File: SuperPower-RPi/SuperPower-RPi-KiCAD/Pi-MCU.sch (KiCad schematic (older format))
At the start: 14 parts, among them J5 Conn_01x06, SW1 Tact, U3 STM32F412RGTx, U4 ATtiny1614-SS, U5 ME6210A33M3G

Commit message: Part Meta-data updates continued.
(cherry picked from commit d0ad2c93dfb1e315a7dc98683a53ed7dcb5f49ff)
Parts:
- added J7: Conn_01x03, symbol Connector_Generic:Conn_01x03
- C25: value 0.1uF -> DNP
- R15: value 10k -> DNP
- U3: Mfg (none) -> ST
- U4: value ATtiny1614-SS -> DNP; Mfg (none) -> MicroChip; Mfg PN (none) -> ATTINY1614-SSFR
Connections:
- net labels removed: Reset
- wire segments 83 -> 92
- no-connect marks 1 -> 0
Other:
- note added: "ATTiny Programming\nVia UPDI"
- note added: "ATtiny1614-SS\n(Optional instead of STM)"
- moved on the sheet: C24, C25, R15, SW1
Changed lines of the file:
@@
 Text HLabel 4950 3000 2    50   BiDi ~ 0
 SCL
-Text HLabel 2350 4100 0    50   BiDi ~ 0
+Text HLabel 3150 3700 0    50   BiDi ~ 0
 GPIO0
-NoConn ~ 2350 4100
 Text Notes 1000 7200 0    50   ~ 0
 Add jumper for measuring MCU current.
@@
 F 2 "Package_QFP:LQFP-64_10x10mm_P0.5mm" H 3500 2000 50  0001 R CNN
 F 3 "http://www.st.com/st-web-ui/static/active/en/resource/technical/document/datasheet/DM00213872.pdf" H 4100 3700 50  0001 C CNN
+F 4 "ST" H 4100 3700 50  0001 C CNN "Mfg"
 	1    4100 3700
-	1    0    0    -1
-$EndComp
-$Comp
-L MCU_Microchip_ATtiny:ATtiny1614-SS U4
-U 1 1 5F9378C2
-P 8750 3950
-F 0 "U4" H 8750 4050 50  0000 C CNN
-F 1 "ATtiny1614-SS" H 8750 3900 50  0000 C CNN
-F 2 "Package_SO:SOIC-14_3.9x8.7mm_P1.27mm" H 8750 3950 50  0001 C CIN
-F 3 "http://ww1.microchip.com/downloads/en/DeviceDoc/ATtiny1614-data-sheet-40001995A.pdf" H 8750 3950 50  0001 C CNN
-	1    8750 3950
 	1    0    0    -1
 $EndComp
@@
 L power:+3.3V #PWR025
 U 1 1 5FA2A2A7
-P 8750 3050
-F 0 "#PWR025" H 8750 2900 50  0001 C CNN
-F 1 "+3.3V" H 8765 3223 50  0000 C CNN
-F 2 "" H 8750 3050 50  0001 C CNN
-F 3 "" H 8750 3050 50  0001 C CNN
-	1    8750 3050
-	1    0    0    -1
-$EndComp
-Wire Wire Line
-	8750 3250 8750 3050
+P 8550 3000
+F 0 "#PWR025" H 8550 2850 50  0001 C CNN
+F 1 "+3.3V" H 8565 3173 50  0000 C CNN
+F 2 "" H 8550 3000 50  0001 C CNN
+F 3 "" H 8550 3000 50  0001 C CNN
+	1    8550 3000
+	1    0    0    -1
+$EndComp
 $Comp
 L Device:C_Small C25
 U 1 1 5FA2B8E5
-P 9250 2900
-F 0 "C25" H 9158 2854 50  0000 R CNN
-F 1 "0.1uF" H 9158 2945 50  0000 R CNN
-F 2 "Capacitor_SMD:C_0603_1608Metric" H 9250 2900 50  0001 C CNN
-F 3 "~" H 9250 2900 50  0001 C CNN
-	1    9250 2900
-	-1   0    0    1
+P 8850 3050
+F 0 "C25" V 8800 3250 50  0000 R CNN
+F 1 "DNP" V 8800 3000 50  0000 R CNN
+F 2 "Capacitor_SMD:C_0603_1608Metric" H 8850 3050 50  0001 C CNN
+F 3 "~" H 8850 3050 50  0001 C CNN
+	1    8850 3050
+	0    -1   1    0
 $EndComp
 $Comp
@@
 L power:GND #PWR026
 U 1 1 5FA2E9B4
-P 8750 4750
-F 0 "#PWR026" H 8750 4500 50  0001 C CNN
-F 1 "GND" H 8755 4577 50  0000 C CNN
-F 2 "" H 8750 4750 50  0001 C CNN
-F 3 "" H 8750 4750 50  0001 C CNN
-	1    8750 4750
-	1    0    0    -1
-$EndComp
-Text HLabel 9600 3650 2    50   BiDi ~ 0
+P 8550 4750
+F 0 "#PWR026" H 8550 4500 50  0001 C CNN
+F 1 "GND" H 8555 4577 50  0000 C CNN
+F 2 "" H 8550 4750 50  0001 C CNN
+F 3 "" H 8550 4750 50  0001 C CNN
+	1    8550 4750
+	1    0    0    -1
+$EndComp
+Text HLabel 9400 3650 2    50   BiDi ~ 0
 SDA
 Wire Wire Line
-	9600 3650 9350 3650
-Text HLabel 9600 3750 2    50   BiDi ~ 0
+	9400 3650 9150 3650
+Text HLabel 9400 3750 2    50   BiDi ~ 0
 SCL
 Wire Wire Line
-	9600 3750 9350 3750
+	9400 3750 9150 3750
 $Comp
 L power:+3.3V #PWR027
 U 1 1 5FA2FF44
-P 9600 3250
-F 0 "#PWR027" H 9600 3100 50  0001 C CNN
-F 1 "+3.3V" H 9615 3423 50  0000 C CNN
-F 2 "" H 9600 3250 50  0001 C CNN
-F 3 "" H 9600 3250 50  0001 C CNN
-	1    9600 3250
+P 9400 3250
+F 0 "#PWR027" H 9400 3100 50  0001 C CNN
+F 1 "+3.3V" H 9415 3423 50  0000 C CNN
+F 2 "" H 9400 3250 50  0001 C CNN
+F 3 "" H 9400 3250 50  0001 C CNN
+	1    9400 3250
 	1    0    0    -1
 $EndComp
@@
 L Device:R_Small R15
 U 1 1 5FA305E2
-P 9600 3400
-F 0 "R15" H 9659 3446 50  0000 L CNN
-F 1 "10k" H 9659 3355 50  0000 L CNN
-F 2 "Resistor_SMD:R_0603_1608Metric" H 9600 3400 50  0001 C CNN
-F 3 "~" H 9600 3400 50  0001 C CNN
-	1    9600 3400
-	1    0    0    -1
-$EndComp
-Wire Wire Line
-	9600 3300 9600 3250
-Wire Wire Line
-	9350 3550 9600 3550
-Wire Wire Line
-	9600 3550 9600 3500
-Wire Wire Line
-	9600 3550 9850 3550
-Connection ~ 9600 3550
-Text Label 9850 3550 0    50   ~ 0
-Reset
-Wire Wire Line
-	8750 4650 8750 4750
-Text HLabel 7750 3900 0    50   BiDi ~ 0
+P 9400 3400
+F 0 "R15" H 9459 3446 50  0000 L CNN
+F 1 "DNP" H 9459 3355 50  0000 L CNN
+F 2 "Resistor_SMD:R_0603_1608Metric" H 9400 3400 50  0001 C CNN
+F 3 "~" H 9400 3400 50  0001 C CNN
+	1    9400 3400
+	1    0    0    -1
+$EndComp
+Wire Wire Line
+	9400 3300 9400 3250
+Wire Wire Line
+	9150 3550 9400 3550
+Wire Wire Line
+	9400 3550 9400 3500
+Wire Wire Line
+	9400 3550 9650 3550
+Connection ~ 9400 3550
+Wire Wire Line
+	8550 4650 8550 4750
+Text HLabel 7550 3900 0    50   BiDi ~ 0
 GPIO0
 Text Label 5250 3500 2    50   ~ 0
@@
 L Switch:SW_Push SW1
 U 1 1 5FA488EA
-P 6700 5500
-F 0 "SW1" V 6746 5452 50  0000 R CNN
-F 1 "Tact" V 6655 5452 50  0000 R CNN
-F 2 "" H 6700 5700 50  0001 C CNN
-F 3 "~" H 6700 5700 50  0001 C CNN
-	1    6700 5500
+P 1200 5750
+F 0 "SW1" V 1246 5702 50  0000 R CNN
+F 1 "Tact" V 1155 5702 50  0000 R CNN
+F 2 "" H 1200 5950 50  0001 C CNN
+F 3 "~" H 1200 5950 50  0001 C CNN
+	1    1200 5750
 	0    -1   -1   0
 $EndComp
@@
 L Device:C_Small C24
 U 1 1 5FA4ADCC
-P 7050 5500
-F 0 "C24" H 6958 5454 50  0000 R CNN
-F 1 "0.1uF" H 6958 5545 50  0000 R CNN
-F 2 "Capacitor_SMD:C_0603_1608Metric" H 7050 5500 50  0001 C CNN
-F 3 "~" H 7050 5500 50  0001 C CNN
-	1    7050 5500
+P 1550 5750
+F 0 "C24" H 1458 5704 50  0000 R CNN
+F 1 "0.1uF" H 1458 5795 50  0000 R CNN
+F 2 "Capacitor_SMD:C_0603_1608Metric" H 1550 5750 50  0001 C CNN
+F 3 "~" H 1550 5750 50  0001 C CNN
+	1    1550 5750
 	-1   0    0    1
 $EndComp
@@
 L power:GND #PWR024
 U 1 1 5FA4B4BE
-P 6800 5900
-F 0 "#PWR024" H 6800 5650 50  0001 C CNN
-F 1 "GND" H 6805 5727 50  0000 C CNN
-F 2 "" H 6800 5900 50  0001 C CNN
-F 3 "" H 6800 5900 50  0001 C CNN
-	1    6800 5900
-	1    0    0    -1
-$EndComp
-Wire Wire Line
-	6800 5900 6800 5800
-Wire Wire Line
-	6800 5800 6700 5800
-Wire Wire Line
-	6700 5800 6700 5700
-Wire Wire Line
-	6800 5800 7050 5800
-Wire Wire Line
-	7050 5800 7050 5600
-Connection ~ 6800 5800
-Text Label 7100 5200 0    50   ~ 0
+P 1300 6150
+F 0 "#PWR024" H 1300 5900 50  0001 C CNN
+F 1 "GND" H 1305 5977 50  0000 C CNN
+F 2 "" H 1300 6150 50  0001 C CNN
+F 3 "" H 1300 6150 50  0001 C CNN
+	1    1300 6150
+	1    0    0    -1
+$EndComp
+Wire Wire Line
+	1300 6150 1300 6050
+Wire Wire Line
+	1300 6050 1200 6050
+Wire Wire Line
+	1200 6050 1200 5950
+Wire Wire Line
+	1300 6050 1550 6050
+Wire Wire Line
+	1550 6050 1550 5850
+Connection ~ 1300 6050
+Text Label 1600 5450 0    50   ~ 0
 nRESET
 Wire Wire Line
-	7050 5400 7050 5200
-Wire Wire Line
-	7050 5200 6700 5200
-Wire Wire Line
-	6700 5200 6700 5300
-Wire Wire Line
-	7100 5200 7050 5200
-Connection ~ 7050 5200
+	1550 5650 1550 5450
+Wire Wire Line
+	1550 5450 1200 5450
+Wire Wire Line
+	1200 5450 1200 5550
+Wire Wire Line
+	1600 5450 1550 5450
+Connection ~ 1550 5450
 Wire Wire Line
 	4400 2000 4400 1900
@@
 Wire Wire Line
 	4150 5600 4100 5600
+$Comp
+L MCU_Microchip_ATtiny:ATtiny1614-SS U4
+U 1 1 5F9378C2
+P 8550 3950
+F 0 "U4" H 8550 4050 50  0000 C CNN
+F 1 "DNP" H 8550 3900 50  0000 C CNN
+F 2 "Package_SO:SOIC-14_3.9x8.7mm_P1.27mm" H 8550 3950 50  0001 C CIN
+F 3 "http://ww1.microchip.com/downloads/en/DeviceDoc/ATtiny1614-data-sheet-40001995A.pdf" H 8550 3950 50  0001 C CNN
+F 4 "MicroChip" H 8550 3950 50  0001 C CNN "Mfg"
+F 5 "ATTINY1614-SSFR" H 8550 3950 50  0001 C CNN "Mfg PN"
+	1    8550 3950
+	1    0    0    -1
+$EndComp
+Text Notes 8300 5250 0    50   ~ 0
+ATtiny1614-SS\n(Optional instead of STM)
+Wire Wire Line
+	8750 3050 8550 3050
+Connection ~ 8550 3050
+Wire Wire Line
+	8550 3050 8550 3000
+$Comp
+L power:GND #PWR029
+U 1 1 5FA31170
+P 9050 3100
+F 0 "#PWR029" H 9050 2850 50  0001 C CNN
+F 1 "GND" H 9055 2927 50  0000 C CNN
+F 2 "" H 9050 3100 50  0001 C CNN
+F 3 "" H 9050 3100 50  0001 C CNN
+	1    9050 3100
+	1    0    0    -1
+$EndComp
+Wire Wire Line
+	8550 3050 8550 3250
+Wire Wire Line
+	9050 3100 9050 3050
+Wire Wire Line
+	9050 3050 8950 3050
+$Comp
+L Connector_Generic:Conn_01x03 J7
+U 1 1 5FA390FB
+P 10550 4900
+F 0 "J7" H 10630 4896 50  0000 L CNN
+F 1 "Conn_01x03" H 10630 4851 50  0001 L CNN
+F 2 "" H 10550 4900 50  0001 C CNN
+F 3 "~" H 10550 4900 50  0001 C CNN
+	1    10550 4900
+	1    0    0    -1
+$EndComp
+$Comp
+L power:GND #PWR031
+U 1 1 5FA3A649
+P 10250 5100
+F 0 "#PWR031" H 10250 4850 50  0001 C CNN
+F 1 "GND" H 10255 4927 50  0000 C CNN
+F 2 "" H 10250 5100 50  0001 C CNN
+F 3 "" H 10250 5100 50  0001 C CNN
+	1    10250 5100
+	1    0    0    -1
+$EndComp
+Wire Wire Line
+	10250 5100 10250 4900
+Wire Wire Line
+	10250 4900 10350 4900
+$Comp
+L power:+3.3V #PWR030
+U 1 1 5FA3CED7
+P 10250 4700
+F 0 "#PWR030" H 10250 4550 50  0001 C CNN
+F 1 "+3.3V" H 10265 4873 50  0000 C CNN
+F 2 "" H 10250 4700 50  0001 C CNN
+F 3 "" H 10250 4700 50  0001 C CNN
+	1    10250 4700
+	1    0    0    -1
+$EndComp
+Wire Wire Line
+	10350 4800 10250 4800
+Wire Wire Line
+	10250 4800 10250 4700
+Wire Wire Line
+	10350 5000 9900 5000
+Text Notes 9950 5600 0    50   ~ 0
+ATTiny Programming\nVia UPDI
+Text Label 9900 5000 0    50   ~ 0
+nRESET
+Text Label 9650 3550 0    50   ~ 0
+nRESET
 $EndSCHEMATC

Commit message: Added local footprint library, and associated components.
(cherry picked from commit 78b1abfd5fe55b90039e798d35239acda24b0417)
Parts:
- added C29, C31: 0.1uF, Capacitor_SMD:C_0603_1608Metric, symbol Device:C_Small
- added C30: 10nF, Capacitor_SMD:C_0603_1608Metric, symbol Device:C_Small
- added C32: 1.0uF, Capacitor_SMD:C_0603_1608Metric, symbol Device:C_Small
- added J8: Conn_01x10, Connector_PinHeader_2.54mm:PinHeader_1x10_P2.54mm_Vertical, symbol Connector_Generic:Conn_01x10
- added R9: 100k, Resistor_SMD:R_0603_1608Metric, symbol Device:R_Small
- added TP4: DNP, TestPoint:TestPoint_Keystone_5000-5004_Miniature, symbol Connector:TestPoint
- J5: footprint (none) -> Connector:Tag-Connect_TC2030-IDC-NL_2x03_P1.27mm_Vertical
- J7: footprint (none) -> Connector_PinHeader_2.54mm:PinHeader_1x03_P2.54mm_Vertical
- SW1: footprint (none) -> Button_Switch_SMD:SW_Push_1P1T-SH_NO_CK_KMR2xxG
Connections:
- wire segments 92 -> 132
- no-connect marks 0 -> 52
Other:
- note added: "Temporary\nBreakout Connections"
- moved on the sheet: C22, C23, C24, C25, J7, R13, R14, R15, SW1, U3

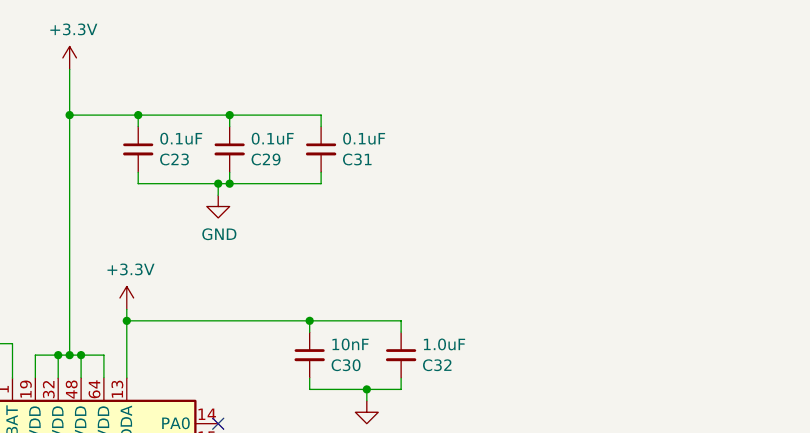
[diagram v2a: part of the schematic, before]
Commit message: Started component grouping and placement on PCB.
(cherry picked from commit c00720279d358cdcfd90ea2d302a0b1b8ef24f40)
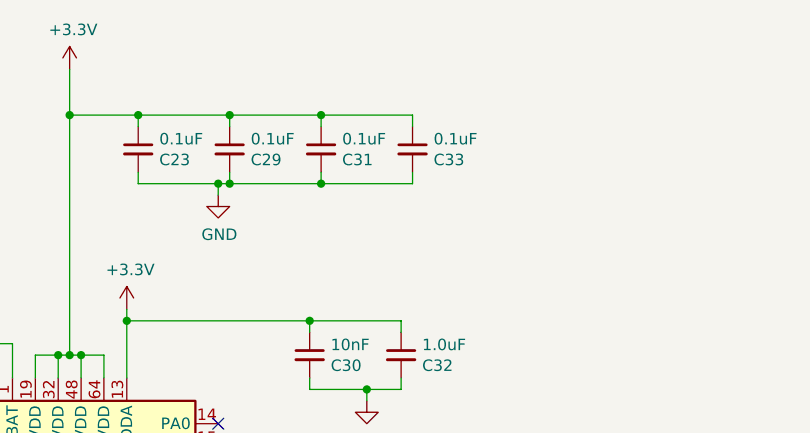
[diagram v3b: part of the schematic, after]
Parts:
- added C33: 0.1uF, Capacitor_SMD:C_0603_1608Metric, symbol Device:C_Small
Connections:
- wire segments 132 -> 136
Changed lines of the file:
@@
 Wire Wire Line
 	3300 2900 3300 2950
+$Comp
+L Device:C_Small C33
+U 1 1 5FA8C003
+P 5650 1350
+F 0 "C33" H 5558 1304 50  0000 R CNN
+F 1 "0.1uF" H 5558 1395 50  0000 R CNN
+F 2 "Capacitor_SMD:C_0603_1608Metric" H 5650 1350 50  0001 C CNN
+F 3 "~" H 5650 1350 50  0001 C CNN
+	1    5650 1350
+	-1   0    0    -1
+$EndComp
+Wire Wire Line
+	5250 1500 5650 1500
+Wire Wire Line
+	5650 1500 5650 1450
+Connection ~ 5250 1500
+Wire Wire Line
+	5650 1250 5650 1200
+Wire Wire Line
+	5650 1200 5250 1200
+Connection ~ 5250 1200
 $EndSCHEMATC

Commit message: Updated components based on 2020/11/08 team meeting.
(cherry picked from commit e5b001aa9b91e1123a0a2394fa23acf6ac376265)
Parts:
- removed TP4: DNP, TestPoint:TestPoint_Keystone_5000-5004_Miniature, symbol Connector:TestPoint
- removed U3: STM32F412RGTx, Package_QFP:LQFP-64_10x10mm_P0.5mm, symbol MCU_ST_STM32F4:STM32F412RGTx
- removed U4: DNP, Package_SO:SOIC-14_3.9x8.7mm_P1.27mm, symbol MCU_Microchip_ATtiny:ATtiny1614-SS
- added J9: Conn_01x02, Connector_PinHeader_2.54mm:PinHeader_1x02_P2.54mm_Vertical, symbol Connector_Generic:Conn_01x02
- added JP1: Jumper_NO_Small, Jumper:SolderJumper-2_P1.3mm_Open_Pad1.0x1.5mm, symbol Device:Jumper_NO_Small
- added R19: DNP, Resistor_SMD:R_0603_1608Metric, symbol Device:R_Small
- added U3: STM32F412RETx, Package_QFP:LQFP-64_10x10mm_P0.5mm, symbol MCU_ST_STM32F4:STM32F412RETx
- added U4: ATtiny85-20SU, Package_SO:SOIJ-8_5.3x5.3mm_P1.27mm, symbol MCU_Microchip_ATtiny:ATtiny85-20SU
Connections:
- net labels added: BOOT0, nRESET_Buf
- wire segments 136 -> 143
- no-connect marks 52 -> 46
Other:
- note added: "ATtiny85-\n(Optional instead of STM)"
- note added: "Swap to Battery Powered"
- note added: "Voltage divider + diode for 5v_RPI measurement"
- note added: "Wire Reset to RPi-GPIO?"
- note removed: "ATtiny1614-SS\n(Optional instead of STM)"
- moved on the sheet: J5, R15

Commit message: Cleaned up schematic a little
(cherry picked from commit 620ad36d41c34f55d759d4c156979e9805418ae0)
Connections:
- net VBAT_REG is gone; now on net +3V3: C21.2, U3.1 (VBAT), U5.3 (OUT)
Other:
- moved on the sheet: J9, JP1
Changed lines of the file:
@@
 Wire Wire Line
 	8250 1350 8250 1500
-$Comp
-L power:+3.3V #PWR017
-U 1 1 5FA249AF
-P 8100 1000
-F 0 "#PWR017" H 8100 850 50  0001 C CNN
-F 1 "+3.3V" H 8115 1173 50  0000 C CNN
-F 2 "" H 8100 1000 50  0001 C CNN
-F 3 "" H 8100 1000 50  0001 C CNN
-	1    8100 1000
-	1    0    0    -1
-$EndComp
 Wire Wire Line
 	8250 1100 8250 1150
@@
 Wire Wire Line
 	4150 2250 4200 2250
-$Comp
-L power:+3.3V #PWR025
-U 1 1 5FA2A2A7
-P 8500 2400
-F 0 "#PWR025" H 8500 2250 50  0001 C CNN
-F 1 "+3.3V" H 8515 2573 50  0000 C CNN
-F 2 "" H 8500 2400 50  0001 C CNN
-F 3 "" H 8500 2400 50  0001 C CNN
-	1    8500 2400
-	1    0    0    -1
-$EndComp
 $Comp
 L Device:C_Small C25
@@
 Text HLabel 1350 1250 0    50   Input ~ 0
 VBAT_IN
-Wire Wire Line
-	3900 2350 3900 2200
-Wire Wire Line
-	3900 2200 3450 2200
-Text Label 3450 2200 0    50   ~ 0
-VBAT_REG
-Text Label 2700 1250 2    50   ~ 0
-VBAT_REG
-Wire Wire Line
-	2300 1250 2700 1250
-Connection ~ 2300 1250
 Wire Wire Line
 	4300 5950 4200 5950
@@
 L Connector_Generic:Conn_01x02 J9
 U 1 1 5FA8EFDB
-P 2300 2650
-F 0 "J9" H 2218 2775 50  0000 C CNN
-F 1 "Conn_01x02" H 2218 2776 50  0001 C CNN
-F 2 "Connector_PinHeader_2.54mm:PinHeader_1x02_P2.54mm_Vertical" H 2300 2650 50  0001 C CNN
-F 3 "~" H 2300 2650 50  0001 C CNN
-	1    2300 2650
+P 2300 2450
+F 0 "J9" H 2218 2575 50  0000 C CNN
+F 1 "Conn_01x02" H 2218 2576 50  0001 C CNN
+F 2 "Connector_PinHeader_2.54mm:PinHeader_1x02_P2.54mm_Vertical" H 2300 2450 50  0001 C CNN
+F 3 "~" H 2300 2450 50  0001 C CNN
+	1    2300 2450
 	-1   0    0    -1
 $EndComp
-$Comp
-L power:+3.3V #PWR036
-U 1 1 5FA9023B
-P 2600 2550
-F 0 "#PWR036" H 2600 2400 50  0001 C CNN
-F 1 "+3.3V" H 2615 2723 50  0000 C CNN
-F 2 "" H 2600 2550 50  0001 C CNN
-F 3 "" H 2600 2550 50  0001 C CNN
-	1    2600 2550
-	1    0    0    -1
-$EndComp
-Wire Wire Line
-	2500 2750 2550 2750
-Wire Wire Line
-	2500 2650 2600 2650
-Wire Wire Line
-	2600 2650 2600 2550
+Wire Wire Line
+	2500 2450 2600 2450
+Wire Wire Line
+	2600 2450 2600 2350
 Text Notes 9650 1900 0    50   ~ 0
 Wire Reset to RPi-GPIO?
-$Comp
-L Device:Jumper_NO_Small JP1
-U 1 1 5FAAD012
-P 2300 2950
-F 0 "JP1" H 2300 3043 50  0000 C CNN
-F 1 "Jumper_NO_Small" H 2300 3044 50  0001 C CNN
-F 2 "Jumper:SolderJumper-2_P1.3mm_Open_Pad1.0x1.5mm" H 2300 2950 50  0001 C CNN
-F 3 "~" H 2300 2950 50  0001 C CNN
-	1    2300 2950
-	1    0    0    -1
-$EndComp
-Wire Wire Line
-	2400 2950 2550 2950
-Wire Wire Line
-	2550 2950 2550 2750
-Connection ~ 2550 2750
-Wire Wire Line
-	2550 2750 2750 2750
 $Comp
 L Device:R_Small R19
@@
 Text Notes 3850 800  0    50   ~ 0
 Swap to Battery Powered
+Text HLabel 2200 2750 0    50   Input ~ 0
+BOOT0
+$Comp
+L Device:Jumper_NO_Small JP1
+U 1 1 5FAAD012
+P 2450 2750
+F 0 "JP1" H 2450 2650 50  0000 C CNN
+F 1 "Jumper_NO_Small" H 2450 2844 50  0001 C CNN
+F 2 "Jumper:SolderJumper-2_P1.3mm_Open_Pad1.0x1.5mm" H 2450 2750 50  0001 C CNN
+F 3 "~" H 2450 2750 50  0001 C CNN
+	1    2450 2750
+	1    0    0    -1
+$EndComp
+Wire Wire Line
+	2550 2750 2600 2750
+Wire Wire Line
+	2500 2550 2600 2550
+Wire Wire Line
+	2600 2550 2600 2750
+Connection ~ 2600 2750
+Wire Wire Line
+	2600 2750 2750 2750
+Wire Wire Line
+	2350 2750 2200 2750
+$Comp
+L power:+3.3V #PWR036
+U 1 1 5FA9023B
+P 2600 2350
+F 0 "#PWR036" H 2600 2200 50  0001 C CNN
+F 1 "+3.3V" H 2615 2523 50  0000 C CNN
+F 2 "" H 2600 2350 50  0001 C CNN
+F 3 "" H 2600 2350 50  0001 C CNN
+	1    2600 2350
+	1    0    0    -1
+$EndComp
+$Comp
+L power:+3.3V #PWR025
+U 1 1 5FA2A2A7
+P 8500 2400
+F 0 "#PWR025" H 8500 2250 50  0001 C CNN
+F 1 "+3.3V" H 8515 2573 50  0000 C CNN
+F 2 "" H 8500 2400 50  0001 C CNN
+F 3 "" H 8500 2400 50  0001 C CNN
+	1    8500 2400
+	1    0    0    -1
+$EndComp
+$Comp
+L power:+3.3V #PWR017
+U 1 1 5FA249AF
+P 8100 1000
+F 0 "#PWR017" H 8100 850 50  0001 C CNN
+F 1 "+3.3V" H 8115 1173 50  0000 C CNN
+F 2 "" H 8100 1000 50  0001 C CNN
+F 3 "" H 8100 1000 50  0001 C CNN
+	1    8100 1000
+	1    0    0    -1
+$EndComp
 $Comp
 L power:+3.3V #PWR033
@@
 	1    0    0    -1
 $EndComp
-Text HLabel 2200 2950 0    50   Input ~ 0
-BOOT0
+$Comp
+L power:+3.3V #PWR?
+U 1 1 5FB90BA7
+P 2450 1150
+F 0 "#PWR?" H 2450 1000 50  0001 C CNN
+F 1 "+3.3V" H 2465 1323 50  0000 C CNN
+F 2 "" H 2450 1150 50  0001 C CNN
+F 3 "" H 2450 1150 50  0001 C CNN
+	1    2450 1150
+	1    0    0    -1
+$EndComp
+Wire Wire Line
+	2450 1250 2450 1150
+$Comp
+L power:+3.3V #PWR?
+U 1 1 5FB98D8D
+P 3900 2150
+F 0 "#PWR?" H 3900 2000 50  0001 C CNN
+F 1 "+3.3V" H 3915 2323 50  0000 C CNN
+F 2 "" H 3900 2150 50  0001 C CNN
+F 3 "" H 3900 2150 50  0001 C CNN
+	1    3900 2150
+	1    0    0    -1
+$EndComp
+Wire Wire Line
+	3900 2150 3900 2350
+Connection ~ 2300 1250
+Wire Wire Line
+	2300 1250 2450 1250
 $EndSCHEMATC
